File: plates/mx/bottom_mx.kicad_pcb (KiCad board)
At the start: 2 copper layers, 273.7 x 107 mm, 12 parts, among them X1 5.5mm, X10 5.5mm, X2 5.5mm, X3 5.5mm, X4 5.5mm, X5 5.5mm, X6 5.5mm, X7 5.5mm, X8 5.5mm, X9 5.5mm

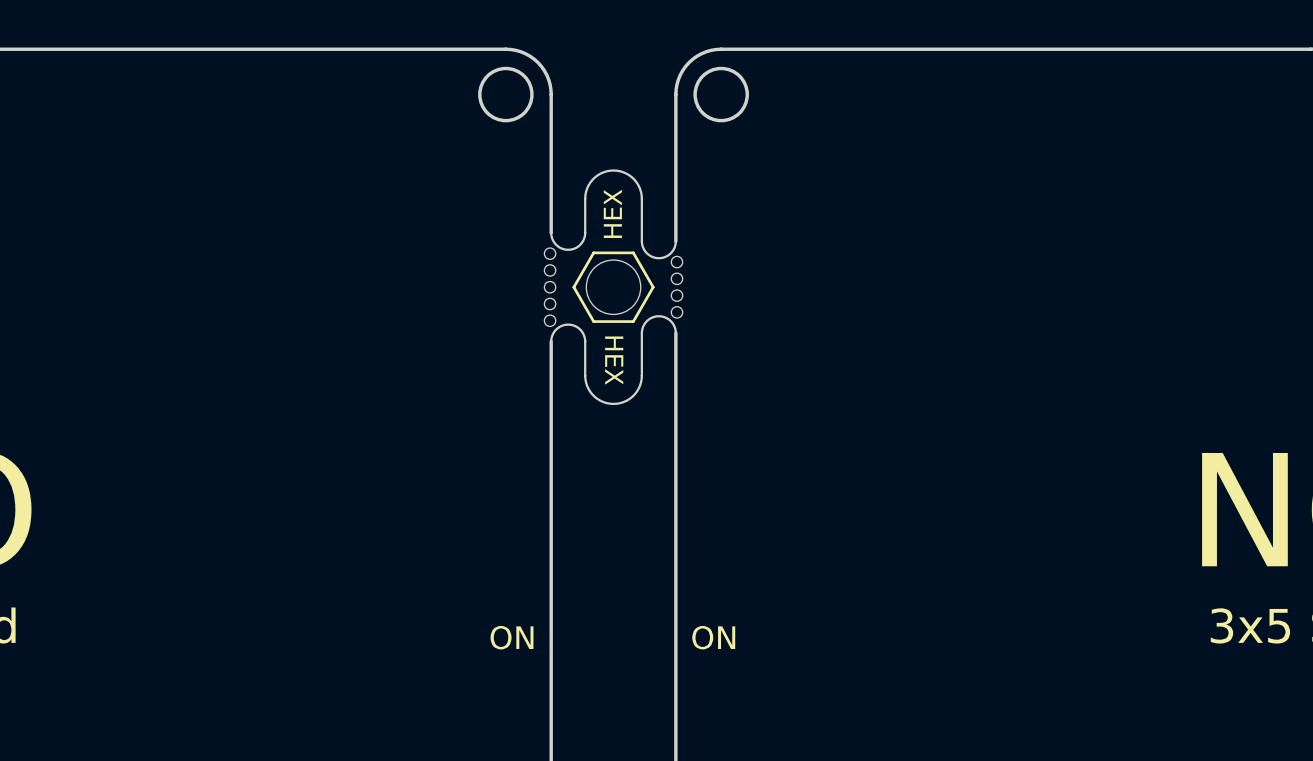
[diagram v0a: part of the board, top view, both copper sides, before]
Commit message: reset switch (#6)
* added reset switch

* Low Profile

pogopin and reset button

* MX Profile

pogopin and reset switch

* MX Profile PCB

* Chimera

pogopin and reset switch

* version

* updated README.md
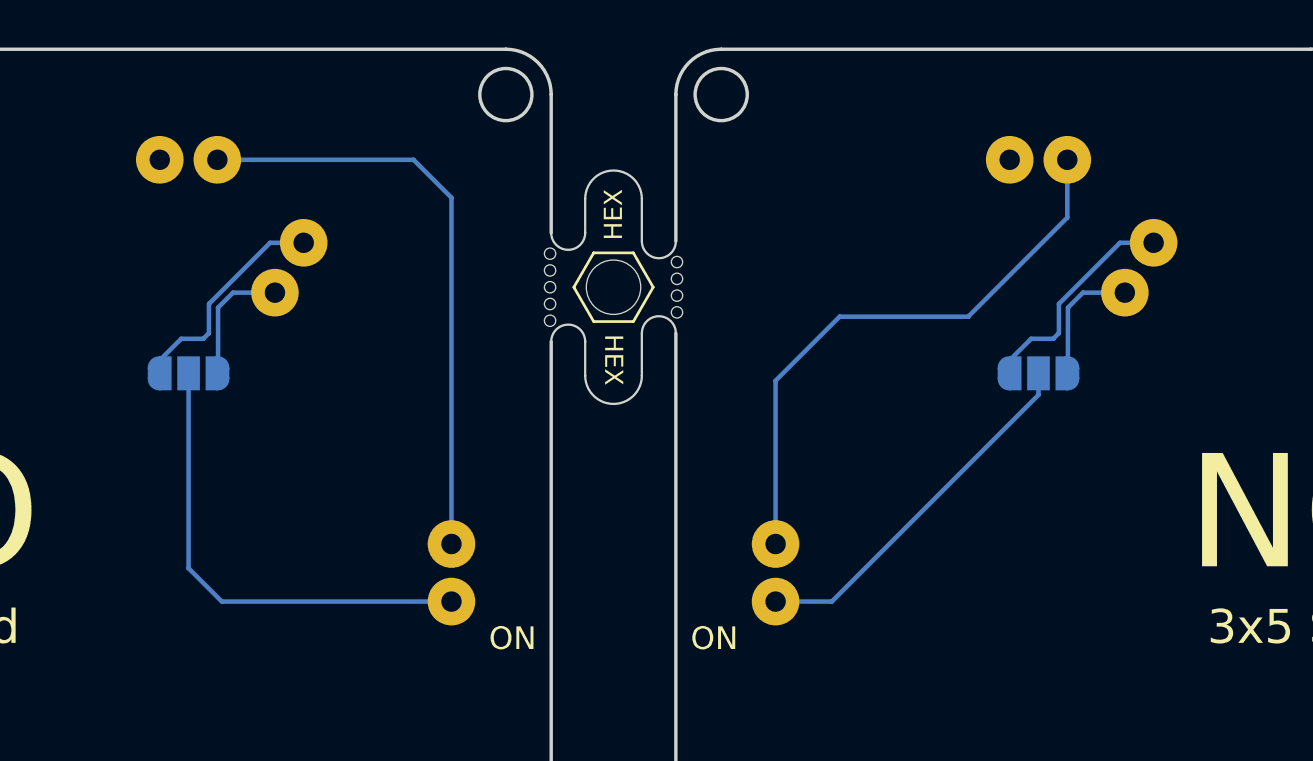
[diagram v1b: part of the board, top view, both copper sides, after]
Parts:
- added J1: Conn_01x02, TB2086_MISC:Pogopin_1x02_P2.54mm, F.Cu at (140.4, 84.1)
- added J2: Conn_01x02, TB2086_MISC:Pogopin_1x02_P2.54mm, F.Cu at (177.9, 84.1)
- added J3: Conn_01x02, TB2086_MISC:Pogopin_1x02_P2.54mm, F.Cu at (136.0, 79.4)
- added J4: Conn_01x02, TB2086_MISC:Pogopin_1x02_P2.54mm, F.Cu at (173.5, 79.4)
- added J5: Conn_01x02, TB2086_MISC:Pogopin_1x02_P2.54mm, F.Cu at (147.6, 97.6)
- added J6: Conn_01x02, TB2086_MISC:Pogopin_1x02_P2.54mm, F.Cu at (161.9, 97.6)
- added JP1: SolderJumper_3_Open, TB2086_MISC:SolderJumper-3_P1.3mm_Open_RoundedPad1.0x1.5mm, F.Cu at (136.0, 88.8)
- added JP2: SolderJumper_3_Open, TB2086_MISC:SolderJumper-3_P1.3mm_Open_RoundedPad1.0x1.5mm, F.Cu at (173.5, 88.8)
- moved X5 169.9 mm to (30.0, 42.5), turned to 90 degrees
- moved X7 169.5 mm to (279.5, 42.5)
- moved X9 88.1 mm to (157.5, 120.0), turned to 0 degrees
- moved X6 80.0 mm to (110.0, 42.5)
- moved X8 80.0 mm to (199.5, 42.5)
- moved X3 69.5 mm to (209.5, 139.5)
- moved X1 60.7 mm to (100.0, 139.5), turned to -90 degrees
- moved X2 40.0 mm to (140.0, 139.5)
- moved X4 40.0 mm to (169.5, 139.5)
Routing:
- net RST: track 0.00 -> 26.3 mm
- net RST_r: track 0.00 -> 25.6 mm
- net BAT: track 0.00 -> 20.8 mm
- net BAT_r: track 0.00 -> 16.3 mm
- net BAT_cr: track 0.00 -> 9.84 mm
- net BAT_c: track 0.00 -> 9.84 mm
- net BAT_xr: track 0.00 -> 5.68 mm
- net BAT_x: track 0.00 -> 5.68 mm
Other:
- board text added: "B+"
- board text added: "GND"
- board text added: "MINI"
- board text added: "RST"
- board text added: "XIAO"

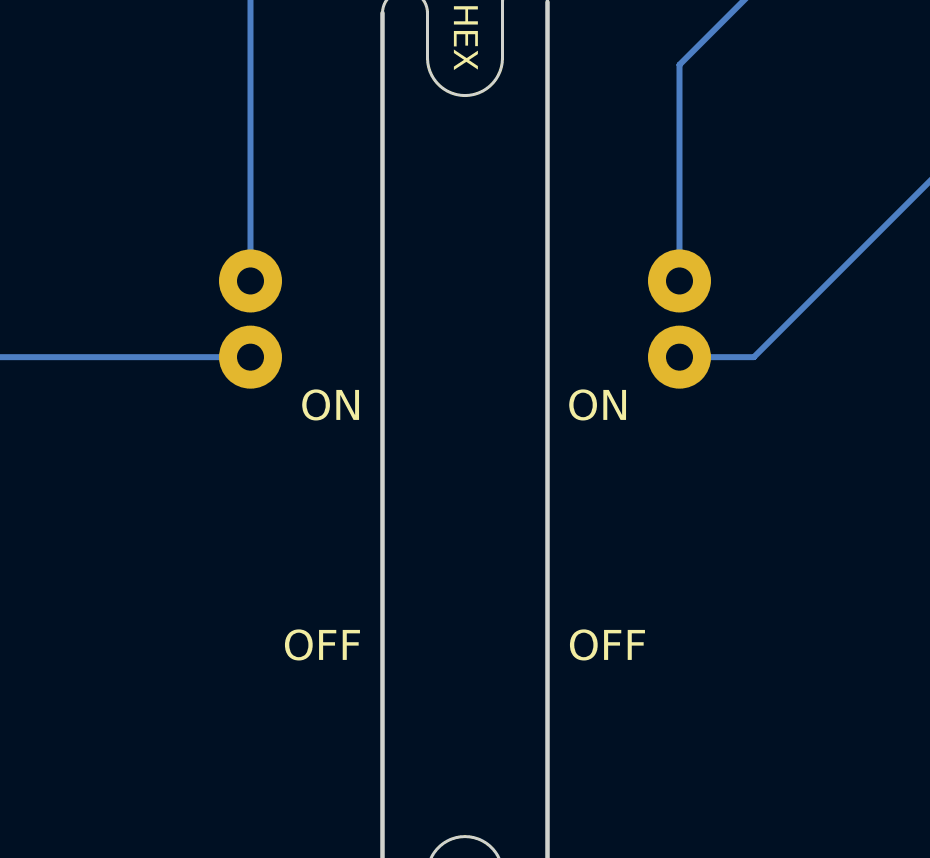
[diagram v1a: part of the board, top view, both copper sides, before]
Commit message: added shells for mx profile
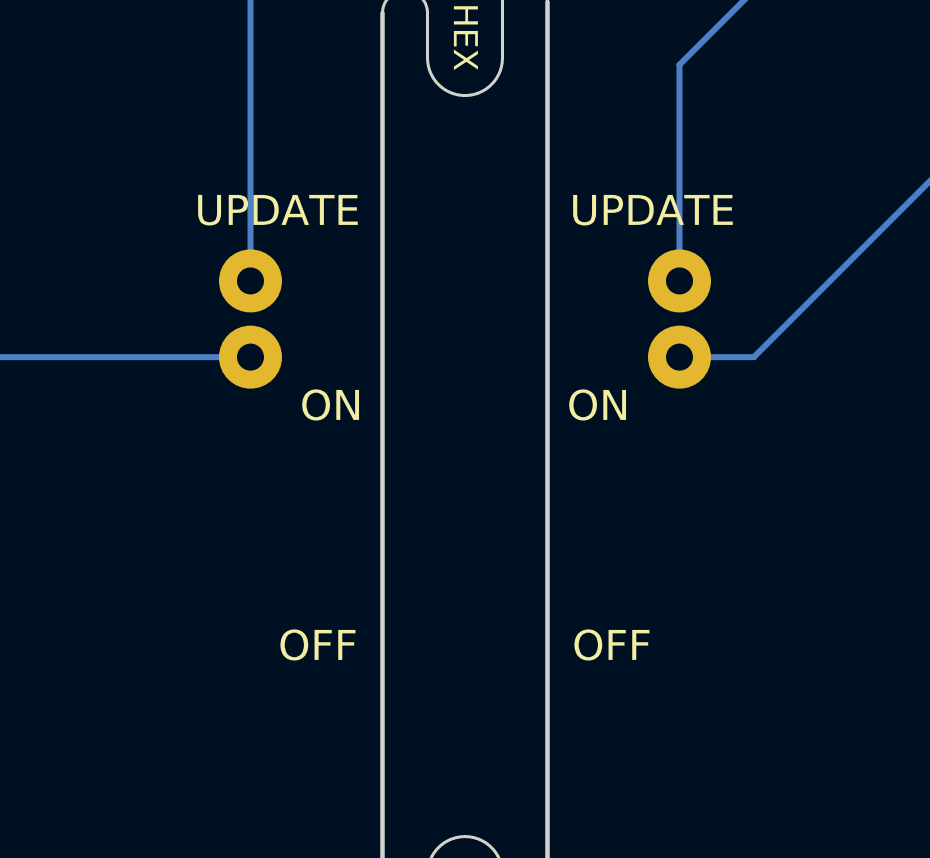
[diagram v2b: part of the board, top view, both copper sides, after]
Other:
- board text added: "UPDATE"
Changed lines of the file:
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@@
-		)
-	)
-	(gr_text "OFF"
-		(at 150 108.5 0)
-		(layer "B.SilkS" knockout)
-		(effects
-			(font
-				(size 1 1)
-				(thickness 0.15)
-			)
-			(justify mirror)
 		)
 	)
@@
 		)
 	)
-	(gr_text "ON"
-		(at 150.3 100.5 0)
-		(layer "B.SilkS" knockout)
-		(effects
-			(font
-				(size 1 1)
-				(thickness 0.15)
-			)
-			(justify mirror)
-		)
-	)
 	(gr_text "MINI"
 		(at 170.5 88.8 -90)
@@
 		)
 	)
-	(gr_text "OFF"
-		(at 159.5 108.5 0)
-		(layer "B.SilkS" knockout)
-		(effects
-			(font
-				(size 1 1)
-				(thickness 0.15)
-			)
-			(justify mirror)
-		)
-	)
 	(gr_text "MX Profile"
 		(at 120 131.5 0)
@@
 				(face "KiCad Font")
 				(size 0.7 0.7)
-				(thickness 0.15)
-			)
-			(justify mirror)
-		)
-	)
-	(gr_text "ON"
-		(at 159.2 100.5 0)
-		(layer "B.SilkS" knockout)
-		(effects
-			(font
-				(size 1 1)
 				(thickness 0.15)
 			)
@@
 	)
 	(gr_text "OFF"
-		(at 159.5 108.5 0)
+		(at 159.65 108.5 0)
 		(layer "F.SilkS" knockout)
 		(effects
@@
 	)
 	(gr_text "OFF"
-		(at 150 108.5 0)
+		(at 149.85 108.5 0)
 		(layer "F.SilkS" knockout)
 		(effects
+			(font
+				(size 1 1)
+				(thickness 0.15)
+			)
+		)
+	)
+	(gr_text "UPDATE"
+		(at 161 94 0)
+		(layer "F.SilkS" knockout)
+		(effects
+			(font
+				(size 1 1)
+				(thickness 0.15)
+			)
+		)
+	)
+	(gr_text "UPDATE"
+		(at 148.5 94 0)
+		(layer "F.SilkS" knockout)
+		(effects
